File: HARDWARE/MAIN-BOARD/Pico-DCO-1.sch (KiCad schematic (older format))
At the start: 21 parts, among them Q1 2N3904, U2 TL074

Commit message: sync
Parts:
- added C?: 100n, Capacitor_THT:C_Rect_L7.2mm_W4.5mm_P5.00mm_FKS2_FKP2_MKS2_MKP2, symbol Device:C
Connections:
- net +12V: now also C5.2; no longer C5.1
- net -12V: now also C?.2; no longer C5.2
- net GND: now also C5.1, C?.1
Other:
- moved on the sheet: C5
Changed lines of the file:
@@
 encoding utf-8
 Sheet 2 7
-Title "TwinTurbo Kosmo > Polykit Raspberry Pi Pico DCO"
+Title "KOSMO-POLY6-PICO-DCO"
 Date "2023-03-06"
-Rev "V0.1.0"
-Comp "Tobin Stage "
+Rev "V0.1.1"
+Comp "Claytune"
 Comment1 "From the Original by Jan Knipper AKA PolyKit  https://github.com/polykit/pico-dco"
 Comment2 "KOSMO-POLY6-PICO-DCO   https://github.com/twinturbo/KOSMO-POLY6-PICO-DCO"
@@
 L Device:C C?
 U 1 1 609307F0
-P 9650 5600
+P 9500 5250
 AR Path="/609307F0" Ref="C?"  Part="1"
 AR Path="/60864F99/609307F0" Ref="C5"  Part="1"
@@
 AR Path="/60AE15A4/609307F0" Ref="C30"  Part="1"
 AR Path="/60AE2DA8/609307F0" Ref="C35"  Part="1"
-F 0 "C5" V 9398 5600 50  0000 C CNN
-F 1 "100n" V 9489 5600 50  0000 C CNN
-F 2 "Capacitor_THT:C_Rect_L7.2mm_W4.5mm_P5.00mm_FKS2_FKP2_MKS2_MKP2" H 9688 5450 50  0001 C CNN
-F 3 "~" H 9650 5600 50  0001 C CNN
-	1    9650 5600
-	1    0    0    -1
-$EndComp
-Wire Wire Line
-	9650 5450 9650 5250
+F 0 "C5" V 9248 5250 50  0000 C CNN
+F 1 "100n" V 9339 5250 50  0000 C CNN
+F 2 "Capacitor_THT:C_Rect_L7.2mm_W4.5mm_P5.00mm_FKS2_FKP2_MKS2_MKP2" H 9538 5100 50  0001 C CNN
+F 3 "~" H 9500 5250 50  0001 C CNN
+	1    9500 5250
+	0    -1   -1   0
+$EndComp
 Wire Wire Line
 	9650 5250 9900 5250
-Wire Wire Line
-	9650 5750 9650 5850
 Wire Wire Line
 	9650 5850 9900 5850
@@
 	-1   0    0    1
 $EndComp
+$Comp
+L power:GND #PWR?
+U 1 1 6406A9A6
+P 9350 5250
+AR Path="/6406A9A6" Ref="#PWR?"  Part="1"
+AR Path="/60864F99/6406A9A6" Ref="#PWR?"  Part="1"
+AR Path="/60A567BE/6406A9A6" Ref="#PWR?"  Part="1"
+AR Path="/60A5EC98/6406A9A6" Ref="#PWR?"  Part="1"
+AR Path="/60A67127/6406A9A6" Ref="#PWR?"  Part="1"
+AR Path="/60A89C21/6406A9A6" Ref="#PWR?"  Part="1"
+AR Path="/60AC3F2C/6406A9A6" Ref="#PWR?"  Part="1"
+AR Path="/60ADE329/6406A9A6" Ref="#PWR?"  Part="1"
+AR Path="/60ADFCBC/6406A9A6" Ref="#PWR?"  Part="1"
+AR Path="/60AE15A4/6406A9A6" Ref="#PWR?"  Part="1"
+AR Path="/60AE2DA8/6406A9A6" Ref="#PWR?"  Part="1"
+F 0 "#PWR?" H 9350 5000 50  0001 C CNN
+F 1 "GND" H 9355 5077 50  0000 C CNN
+F 2 "" H 9350 5250 50  0001 C CNN
+F 3 "" H 9350 5250 50  0001 C CNN
+	1    9350 5250
+	0    1    1    0
+$EndComp
+$Comp
+L Device:C C?
+U 1 1 6406F6CF
+P 9500 5850
+AR Path="/6406F6CF" Ref="C?"  Part="1"
+AR Path="/60864F99/6406F6CF" Ref="C?"  Part="1"
+AR Path="/60A567BE/6406F6CF" Ref="C?"  Part="1"
+AR Path="/60A5EC98/6406F6CF" Ref="C?"  Part="1"
+AR Path="/60A67127/6406F6CF" Ref="C?"  Part="1"
+AR Path="/60A89C21/6406F6CF" Ref="C?"  Part="1"
+AR Path="/60AC3F2C/6406F6CF" Ref="C?"  Part="1"
+AR Path="/60ADE329/6406F6CF" Ref="C?"  Part="1"
+AR Path="/60ADFCBC/6406F6CF" Ref="C?"  Part="1"
+AR Path="/60AE15A4/6406F6CF" Ref="C?"  Part="1"
+AR Path="/60AE2DA8/6406F6CF" Ref="C?"  Part="1"
+F 0 "C?" V 9248 5850 50  0000 C CNN
+F 1 "100n" V 9339 5850 50  0000 C CNN
+F 2 "Capacitor_THT:C_Rect_L7.2mm_W4.5mm_P5.00mm_FKS2_FKP2_MKS2_MKP2" H 9538 5700 50  0001 C CNN
+F 3 "~" H 9500 5850 50  0001 C CNN
+	1    9500 5850
+	0    -1   -1   0
+$EndComp
+$Comp
+L power:GND #PWR?
+U 1 1 6406FA87
+P 9350 5850
+AR Path="/6406FA87" Ref="#PWR?"  Part="1"
+AR Path="/60864F99/6406FA87" Ref="#PWR?"  Part="1"
+AR Path="/60A567BE/6406FA87" Ref="#PWR?"  Part="1"
+AR Path="/60A5EC98/6406FA87" Ref="#PWR?"  Part="1"
+AR Path="/60A67127/6406FA87" Ref="#PWR?"  Part="1"
+AR Path="/60A89C21/6406FA87" Ref="#PWR?"  Part="1"
+AR Path="/60AC3F2C/6406FA87" Ref="#PWR?"  Part="1"
+AR Path="/60ADE329/6406FA87" Ref="#PWR?"  Part="1"
+AR Path="/60ADFCBC/6406FA87" Ref="#PWR?"  Part="1"
+AR Path="/60AE15A4/6406FA87" Ref="#PWR?"  Part="1"
+AR Path="/60AE2DA8/6406FA87" Ref="#PWR?"  Part="1"
+F 0 "#PWR?" H 9350 5600 50  0001 C CNN
+F 1 "GND" H 9355 5677 50  0000 C CNN
+F 2 "" H 9350 5850 50  0001 C CNN
+F 3 "" H 9350 5850 50  0001 C CNN
+	1    9350 5850
+	0    1    1    0
+$EndComp
 $EndSCHEMATC

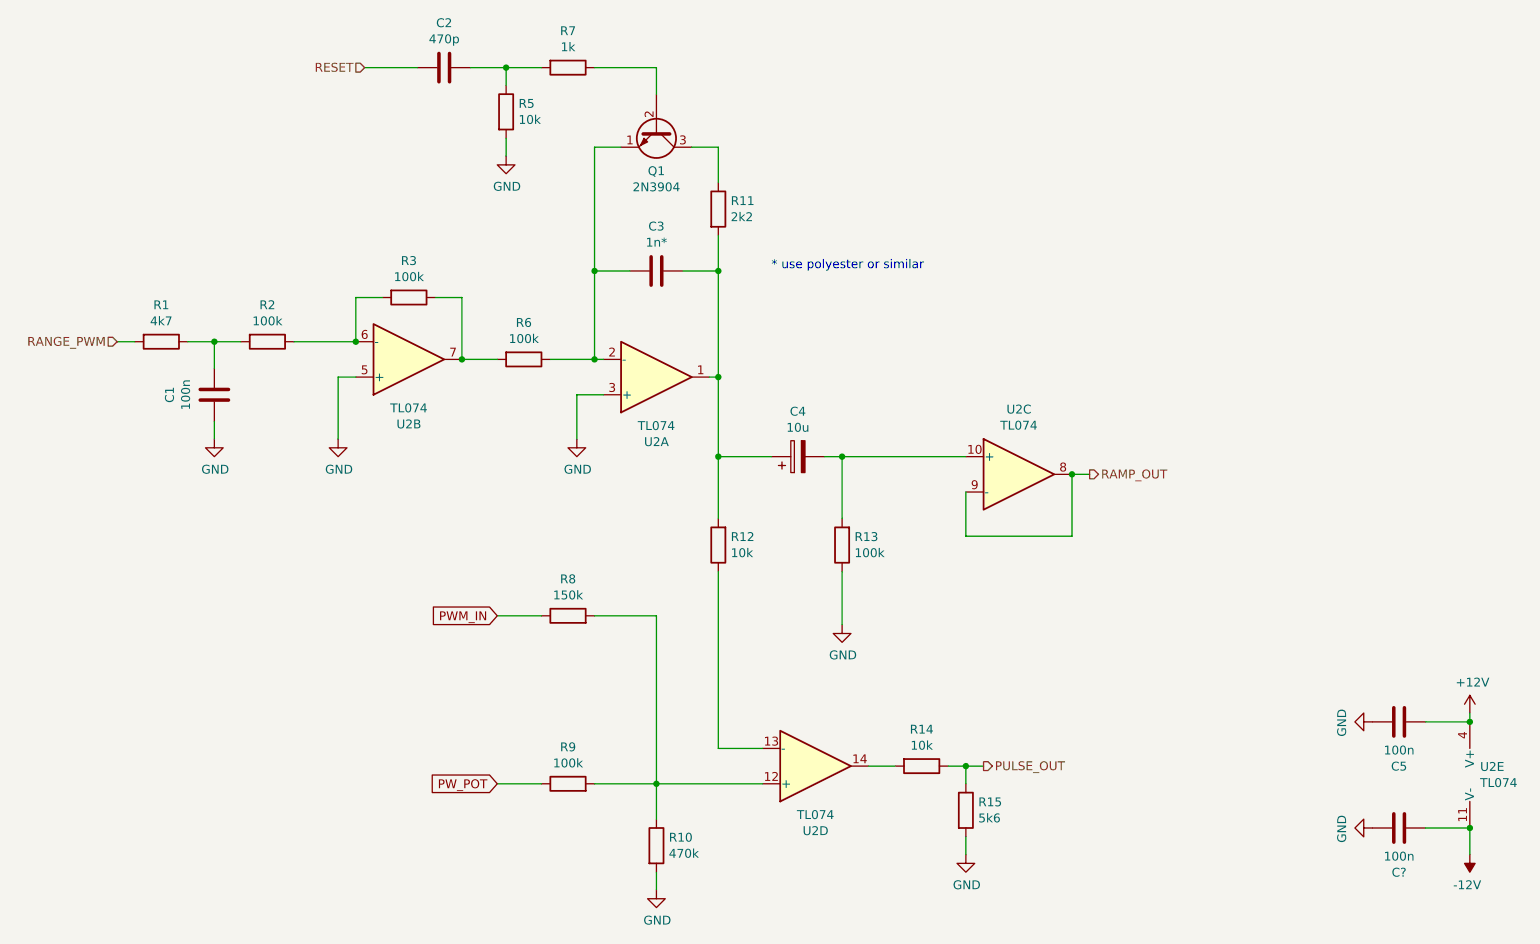
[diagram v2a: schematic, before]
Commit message: Added jumper on PWM pot to go to future PG Programmer
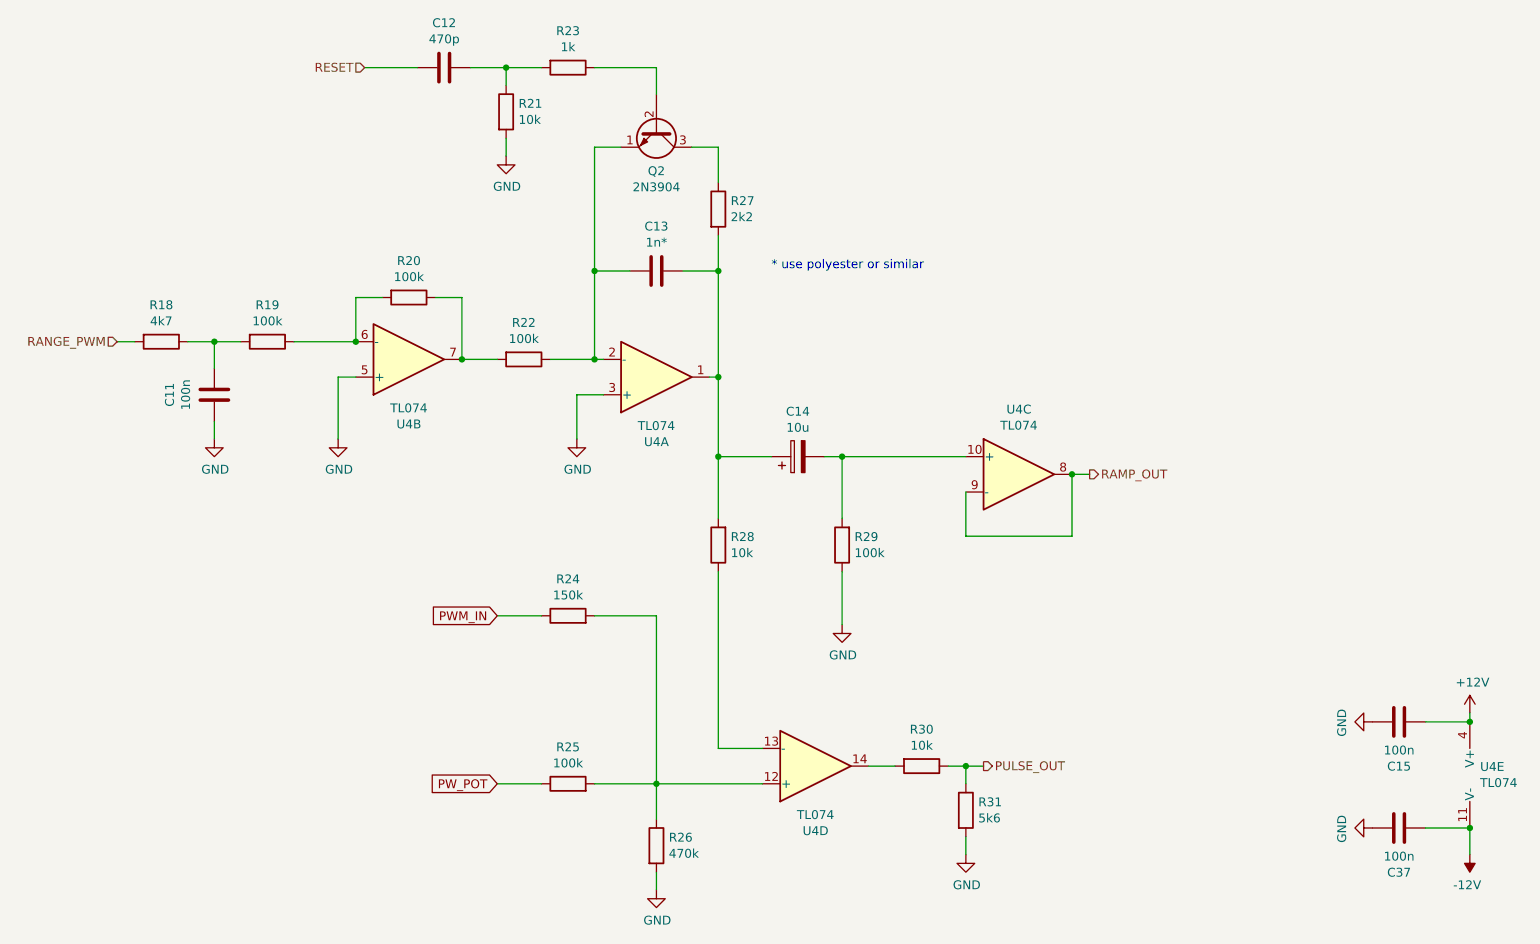
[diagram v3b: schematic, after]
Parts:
- gave numbers to parts that had none: 1
